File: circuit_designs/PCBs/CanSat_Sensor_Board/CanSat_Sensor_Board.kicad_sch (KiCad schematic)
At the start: 24 parts

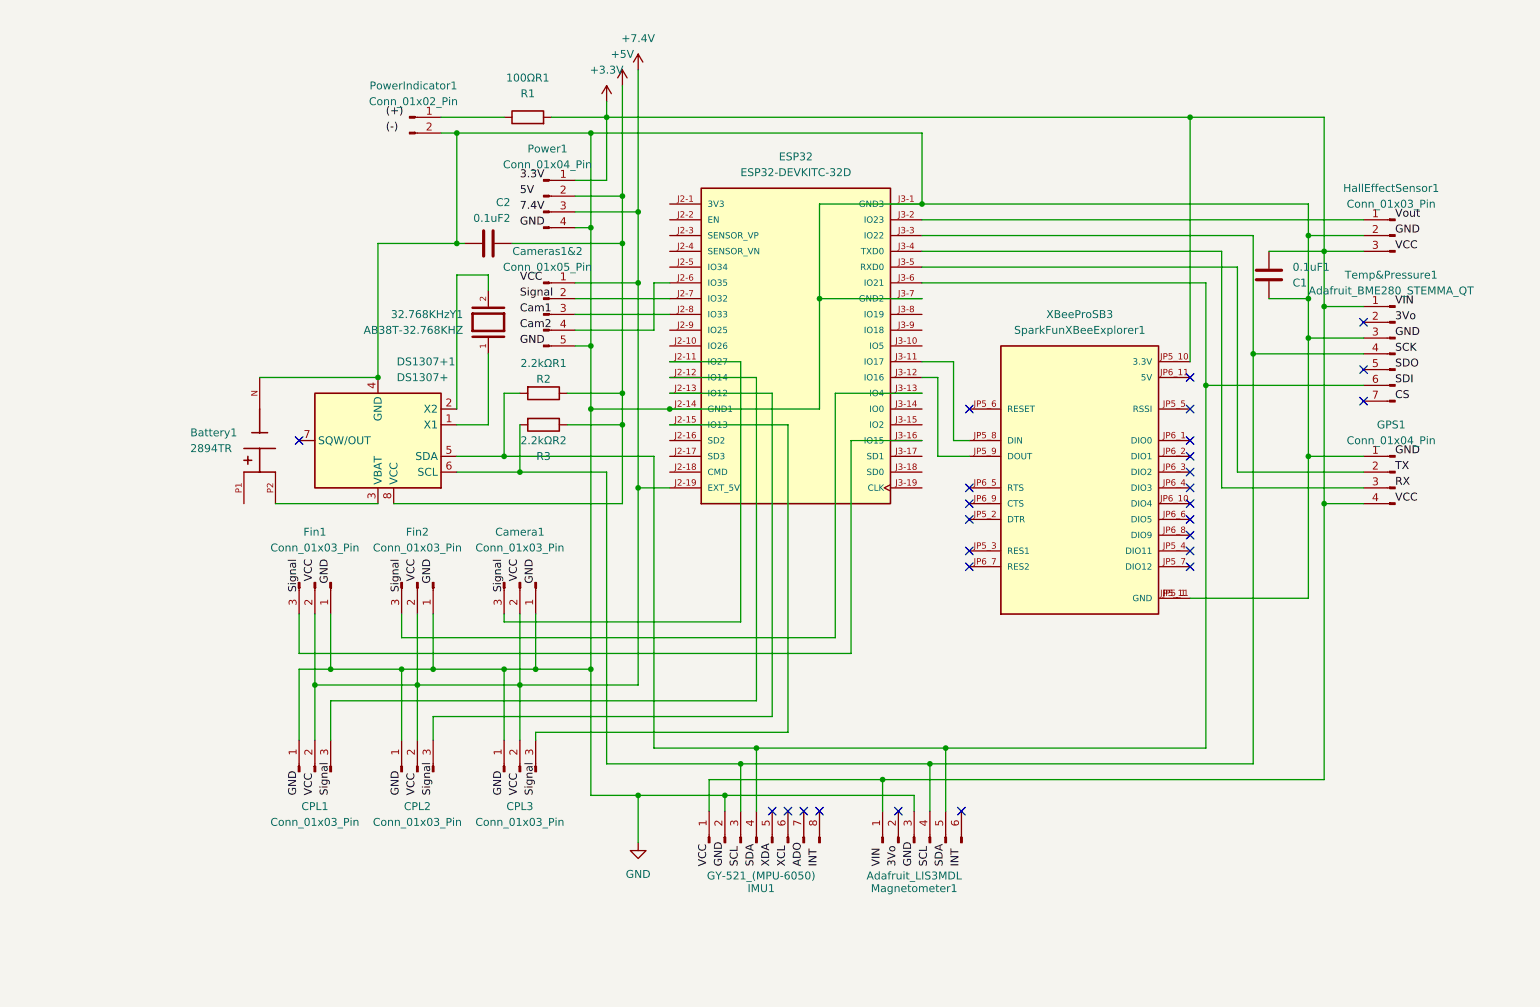
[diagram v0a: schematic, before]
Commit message: Updating camera and sensor PCBs
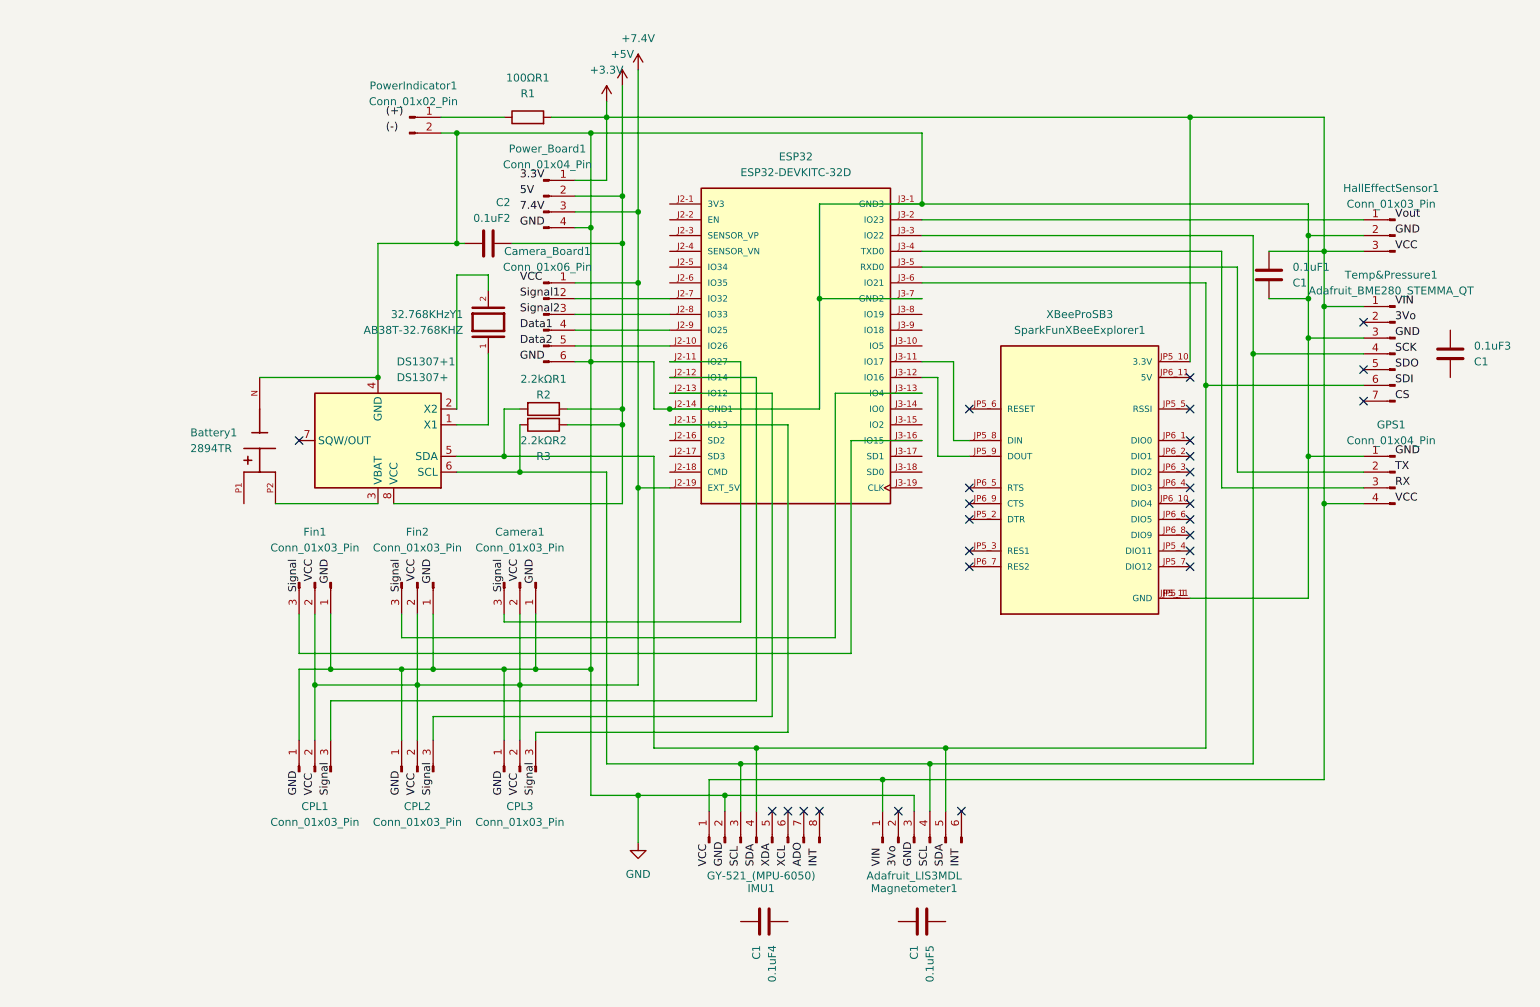
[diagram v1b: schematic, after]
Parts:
- removed Cameras1&2: Conn_01x05_Pin, Connector_JST:JST_PH_B5B-PH-K_1x05_P2.00mm_Vertical, symbol Connector:Conn_01x05_Pin
- added 0.1uF3, 0.1uF4, 0.1uF5: C1, Capacitor_SMD:C_0805_2012Metric_Pad1.18x1.45mm_HandSolder, symbol Device:C
- added Camera_Board1: Conn_01x06_Pin, Connector_JST:JST_PH_B6B-PH-K_1x06_P2.00mm_Vertical, symbol Connector:Conn_01x06_Pin
- XBeeProSB3: footprint WRL-11812:MODULE_WRL-11812 -> Custom_Footprints:SparkFun_XBee_Explorer_Regulated
- renumbered Power1 to Power_Board1
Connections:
- net +7.4V: now also Camera_Board1.1 (Pin_1)
- net GND: now also Camera_Board1.6 (Pin_6)
- net at ESP32.J2-7 (IO32): now also Camera_Board1.2 (Pin_2)
- net at ESP32.J2-8 (IO33): now also Camera_Board1.3 (Pin_3)
- net at ESP32.J2-10 (IO26): now also Camera_Board1.5 (Pin_5)
- net at ESP32.J2-9 (IO25): now also Camera_Board1.4 (Pin_4)
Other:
- moved on the sheet: 2.2kΩR1

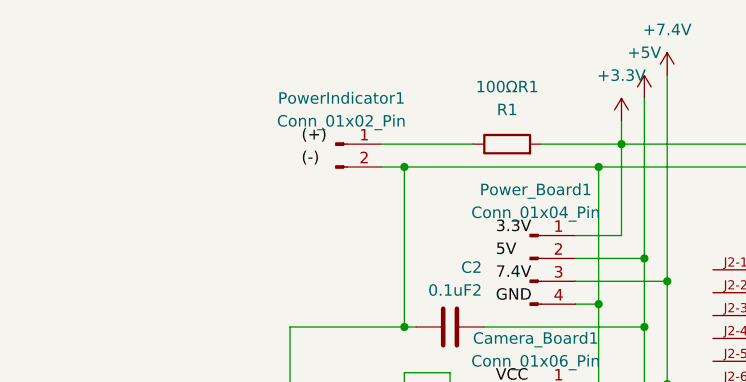
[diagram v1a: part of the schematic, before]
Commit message: Updating new KiCad files
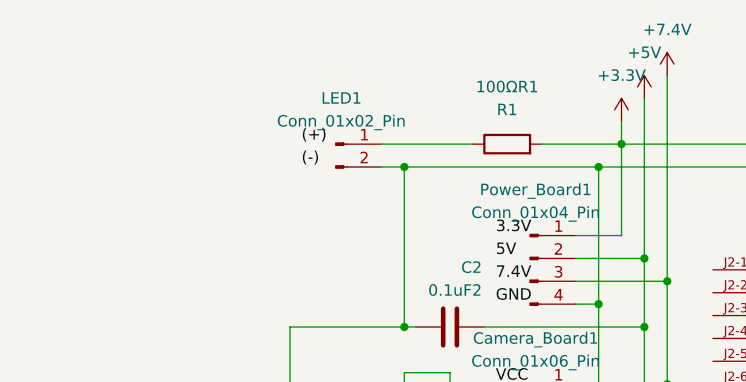
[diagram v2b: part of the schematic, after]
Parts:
- renumbered PowerIndicator1 to LED1
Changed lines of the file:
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@@
 		(dnp no)
 		(fields_autoplaced yes)
-		(property "Reference" "PowerIndicator1"
+		(property "Reference" "LED1"
 			(at 83.185 48.26 0)
 			(effects
@@
 			(project ""
 				(path "/f8796b72-1214-4476-868c-7fa3fa666d69"
-					(reference "PowerIndicator1")
+					(reference "LED1")
 					(unit 1)
 				)

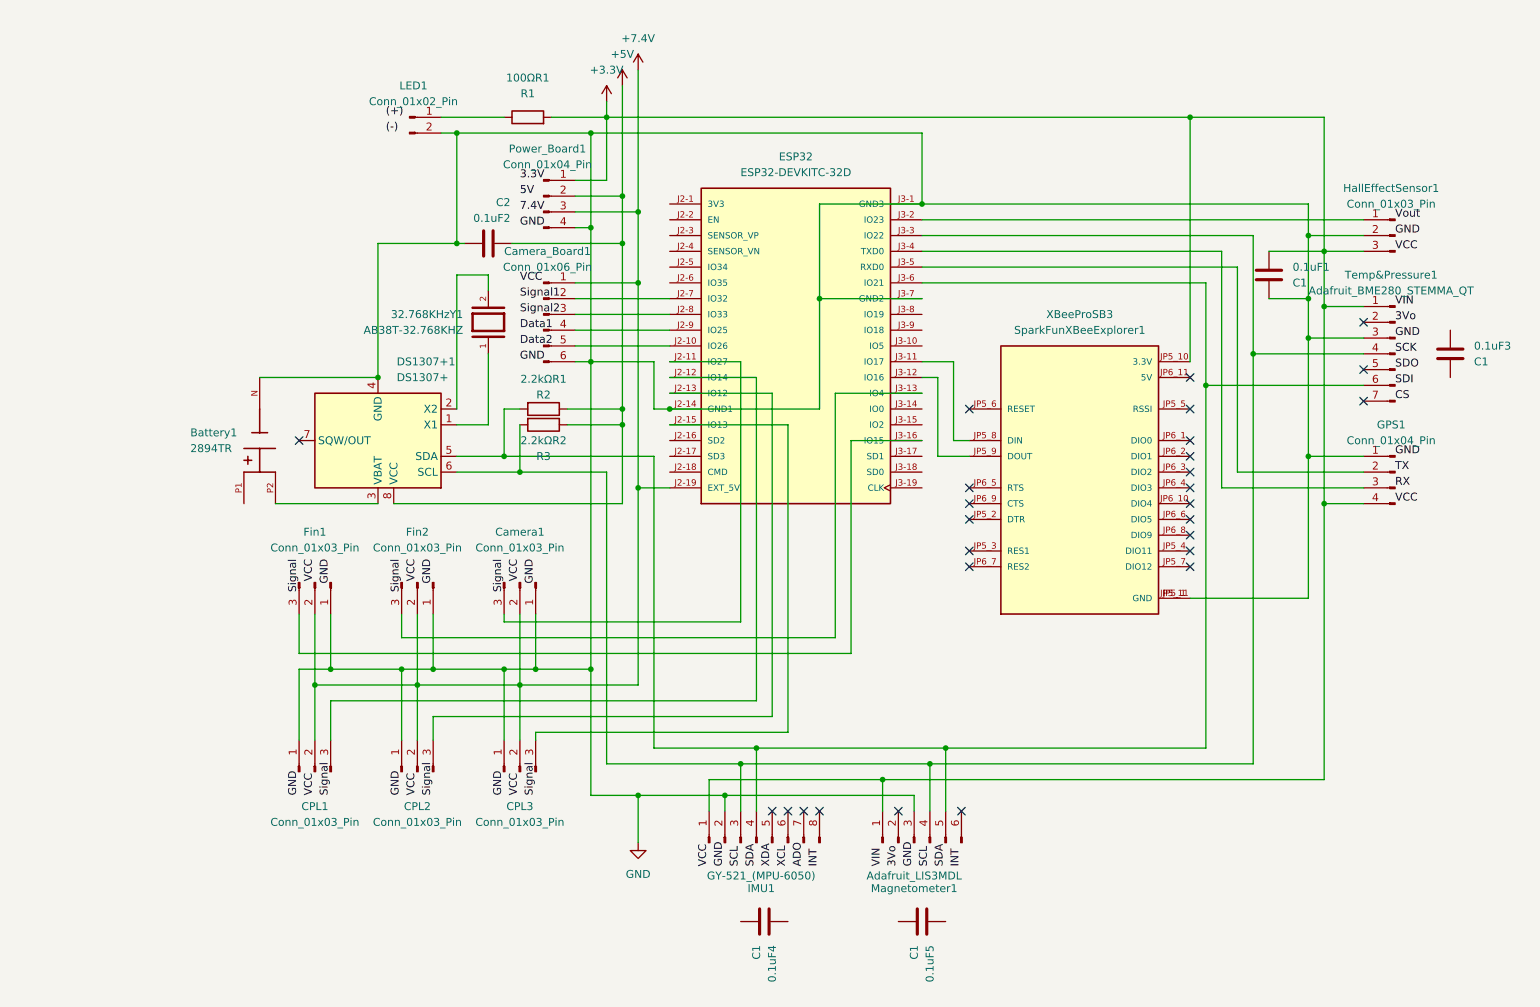
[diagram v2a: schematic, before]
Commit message: Final review submission of all CanSat PCB boards and corresponding custom KiCad 3D models, footprints, and symbols
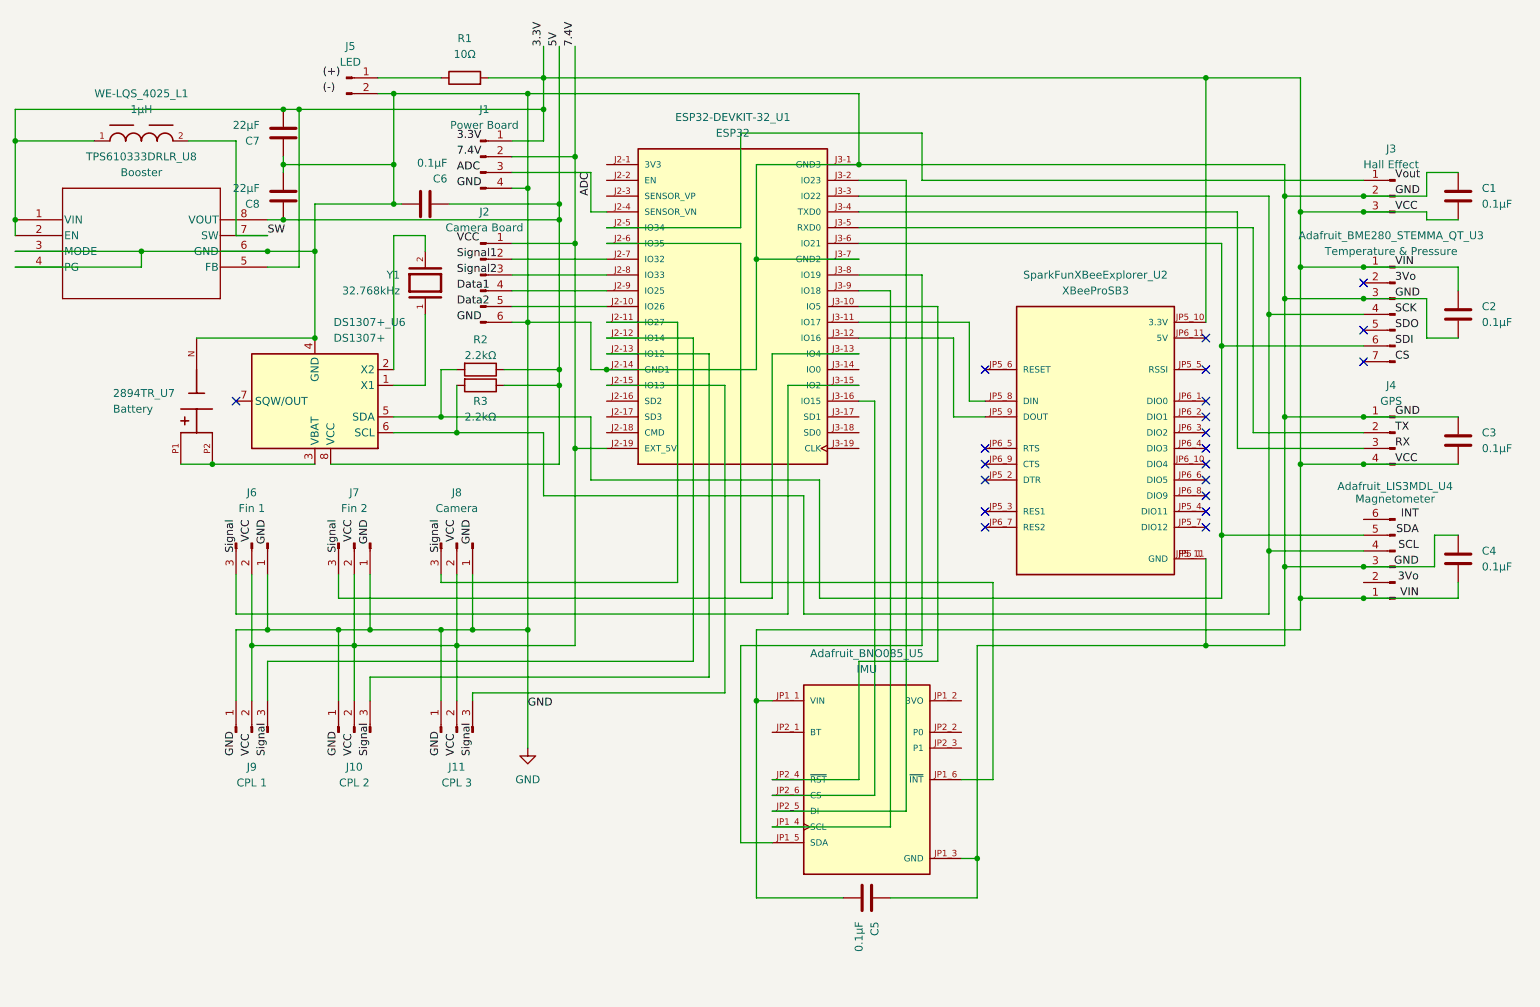
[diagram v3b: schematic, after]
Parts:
- removed IMU1: GY-521_(MPU-6050), Custom_Footprints:GY-521_(MPU-6050), symbol Connector:Conn_01x08_Pin
- added Adafruit_BNO085_U5: IMU, Custom_Footprints:Adafruit_BNO085, symbol 4754:4754
- added C3: 0.1μF, Capacitor_SMD:C_0805_2012Metric_Pad1.18x1.45mm_HandSolder, symbol Device:C
- added C7, C8: 22μF, Capacitor_SMD:C_0805_2012Metric_Pad1.18x1.45mm_HandSolder, symbol Device:C
- added TPS610333DRLR_U8: Booster, DigiKey:SOT-5X3-8_DRL_TEX, symbol TPS610333DRLR:TPS610333DRLR
- added WE-LQS_4025_L1: 1μH, DigiKey:WE-LQS_4025, symbol WE-LQS_4025:WE-LQS_4025
- 2894TR_U7: renamed from Battery1; value 2894TR -> Battery
- Adafruit_BME280_STEMMA_QT_U3: renamed from Temp&Pressure1; value Adafruit_BME280_STEMMA_QT -> Temperature & Pressure
- Adafruit_LIS3MDL_U4: renamed from Magnetometer1; value Adafruit_LIS3MDL -> Magnetometer
- C1: renamed from 0.1uF1; value C1 -> 0.1μF
- C2: renamed from 0.1uF3; value C1 -> 0.1μF
- C4: renamed from 0.1uF5; value C1 -> 0.1μF
- C5: renamed from 0.1uF4; value C1 -> 0.1μF
- C6: renamed from 0.1uF2; value C2 -> 0.1μF
- ESP32-DEVKIT-32_U1: renamed from ESP32; value ESP32-DEVKITC-32D -> ESP32
- J1: renamed from Power_Board1; value Conn_01x04_Pin -> Power Board
- J10: renamed from CPL2; value Conn_01x03_Pin -> CPL 2
- J11: renamed from CPL3; value Conn_01x03_Pin -> CPL 3
- J2: renamed from Camera_Board1; value Conn_01x06_Pin -> Camera Board
- J3: renamed from HallEffectSensor1; value Conn_01x03_Pin -> Hall Effect
- J4: renamed from GPS1; value Conn_01x04_Pin -> GPS
- J5: renamed from LED1; value Conn_01x02_Pin -> LED
- J6: renamed from Fin1; value Conn_01x03_Pin -> Fin 1
- J7: renamed from Fin2; value Conn_01x03_Pin -> Fin 2
- J8: renamed from Camera1; value Conn_01x03_Pin -> Camera
- J9: renamed from CPL1; value Conn_01x03_Pin -> CPL 1
- R1: renamed from 100ΩR1; value R1 -> 10Ω; footprint Resistor_THT:R_Axial_DIN0207_L6.3mm_D2.5mm_P7.62mm_Horizontal -> Resistor_SMD:R_0603_1608Metric_Pad0.98x0.95mm_HandSolder
- R2: renamed from 2.2kΩR1; value R2 -> 2.2kΩ
- R3: renamed from 2.2kΩR2; value R3 -> 2.2kΩ
- SparkFunXBeeExplorer_U2: renamed from XBeeProSB3; value SparkFunXBeeExplorer1 -> XBeeProSB3
- Y1: renamed from 32.768KHzY1; value AB38T-32.768KHZ -> 32.768kHz
- renumbered DS1307+1 to DS1307+_U6
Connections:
- net 3.3V: now also Adafruit_BME280_STEMMA_QT_U3.1 (Pin_1), Adafruit_LIS3MDL_U4.1 (Pin_1), C1.2, C2.1, C4.2, C5.2, J1.1 (Pin_1), J3.3 (Pin_3), J4.4 (Pin_4), R1.2, SparkFunXBeeExplorer_U2.JP5_10 (3.3V), Adafruit_BNO085_U5.JP1_1 (VIN), C3.2, C7.2, TPS610333DRLR_U8.1 (VIN), TPS610333DRLR_U8.2 (EN), TPS610333DRLR_U8.5 (FB), WE-LQS_4025_L1.1
- net 5V: now also C6.2, DS1307+_U6.8 (VCC), R2.1, R3.1, C8.1, TPS610333DRLR_U8.8 (VOUT)
- net 7.4V: now also ESP32-DEVKIT-32_U1.J2-19 (EXT_5V), J1.2 (Pin_2), J10.2 (Pin_2), J11.2 (Pin_2), J2.1 (Pin_1), J6.2 (Pin_2), J7.2 (Pin_2), J8.2 (Pin_2), J9.2 (Pin_2)
- net GND: now also C1.1, C2.2, C4.1, C5.1, Adafruit_BNO085_U5.JP1_3 (GND), C3.1, C7.1, C8.2, TPS610333DRLR_U8.3 (MODE), TPS610333DRLR_U8.4 (PG), TPS610333DRLR_U8.6 (GND); no longer C1.2
- net at J3.1 (Pin_1): now also ESP32-DEVKIT-32_U1.J2-5 (IO34); no longer ESP32-DEVKIT-32_U1.J3-2 (IO23)
- net at 2894TR_U7.P1: now also 2894TR_U7.P2, DS1307+_U6.3 (VBAT)
- net at J6.3 (Pin_3): now also ESP32-DEVKIT-32_U1.J3-15 (IO2); no longer ESP32-DEVKIT-32_U1.J3-16 (IO15)
- net ADC: now reaches ESP32-DEVKIT-32_U1.J2-4 (SENSOR_VN)
- net ADC: now also J1.3 (Pin_3)
- net at ESP32-DEVKIT-32_U1.J2-6 (IO35): now also Adafruit_BNO085_U5.JP1_6 (~{INT})
- net at ESP32-DEVKIT-32_U1.J3-10 (IO5): now also Adafruit_BNO085_U5.JP2_4 (~{RST})
- net at ESP32-DEVKIT-32_U1.J3-8 (IO19): now also Adafruit_BNO085_U5.JP1_5 (SDA)
- net at ESP32-DEVKIT-32_U1.J3-9 (IO18): now also Adafruit_BNO085_U5.JP1_4 (SCL)
- removed net +3.3V: Adafruit_BME280_STEMMA_QT_U3.1 (Pin_1), Adafruit_LIS3MDL_U4.1 (Pin_1), C1.1, J1.1 (Pin_1), J3.3 (Pin_3), J4.4 (Pin_4), R1.2, SparkFunXBeeExplorer_U2.JP5_10 (3.3V)
- removed net +5V: C6.2, DS1307+_U6.8 (VCC), J1.2 (Pin_2), R2.1, R3.1
- removed net +7.4V: ESP32-DEVKIT-32_U1.J2-19 (EXT_5V), J1.3 (Pin_3), J10.2 (Pin_2), J11.2 (Pin_2), J2.1 (Pin_1), J6.2 (Pin_2), J7.2 (Pin_2), J8.2 (Pin_2), J9.2 (Pin_2)
- new net: Adafruit_BNO085_U5.JP2_6 (CS), ESP32-DEVKIT-32_U1.J3-16 (IO15)
- new net: Adafruit_BNO085_U5.JP2_5 (DI), ESP32-DEVKIT-32_U1.J3-2 (IO23)
- new net SW: TPS610333DRLR_U8.7 (SW), WE-LQS_4025_L1.2
- no-connect marks 27 -> 21
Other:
- moved on the sheet: 2894TR_U7, Adafruit_BME280_STEMMA_QT_U3, Adafruit_LIS3MDL_U4, C1, C2, C4, C5, C6, DS1307+_U6, ESP32-DEVKIT-32_U1, J1, J10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
